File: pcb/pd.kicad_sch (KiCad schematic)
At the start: 28 parts, among them J7 Conn_01x02, U10 SGM6602-12, U11 HX4054A, U12 BQ27220, U8 TPS63051RMWR, U9 PCA9410AUKZ

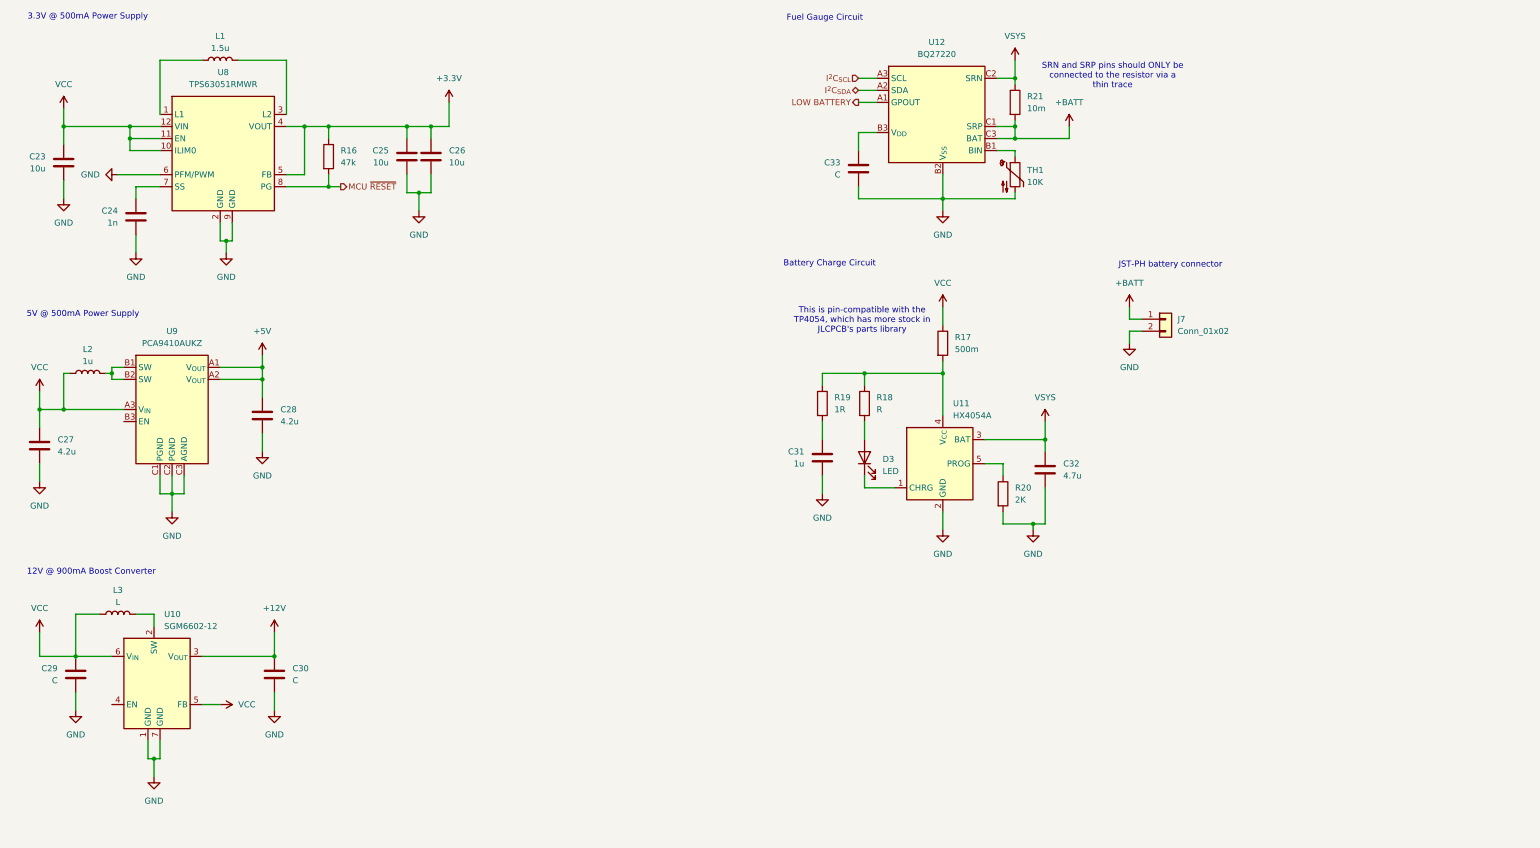
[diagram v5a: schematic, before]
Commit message: feat: revised 3.3v power rail, added power switch
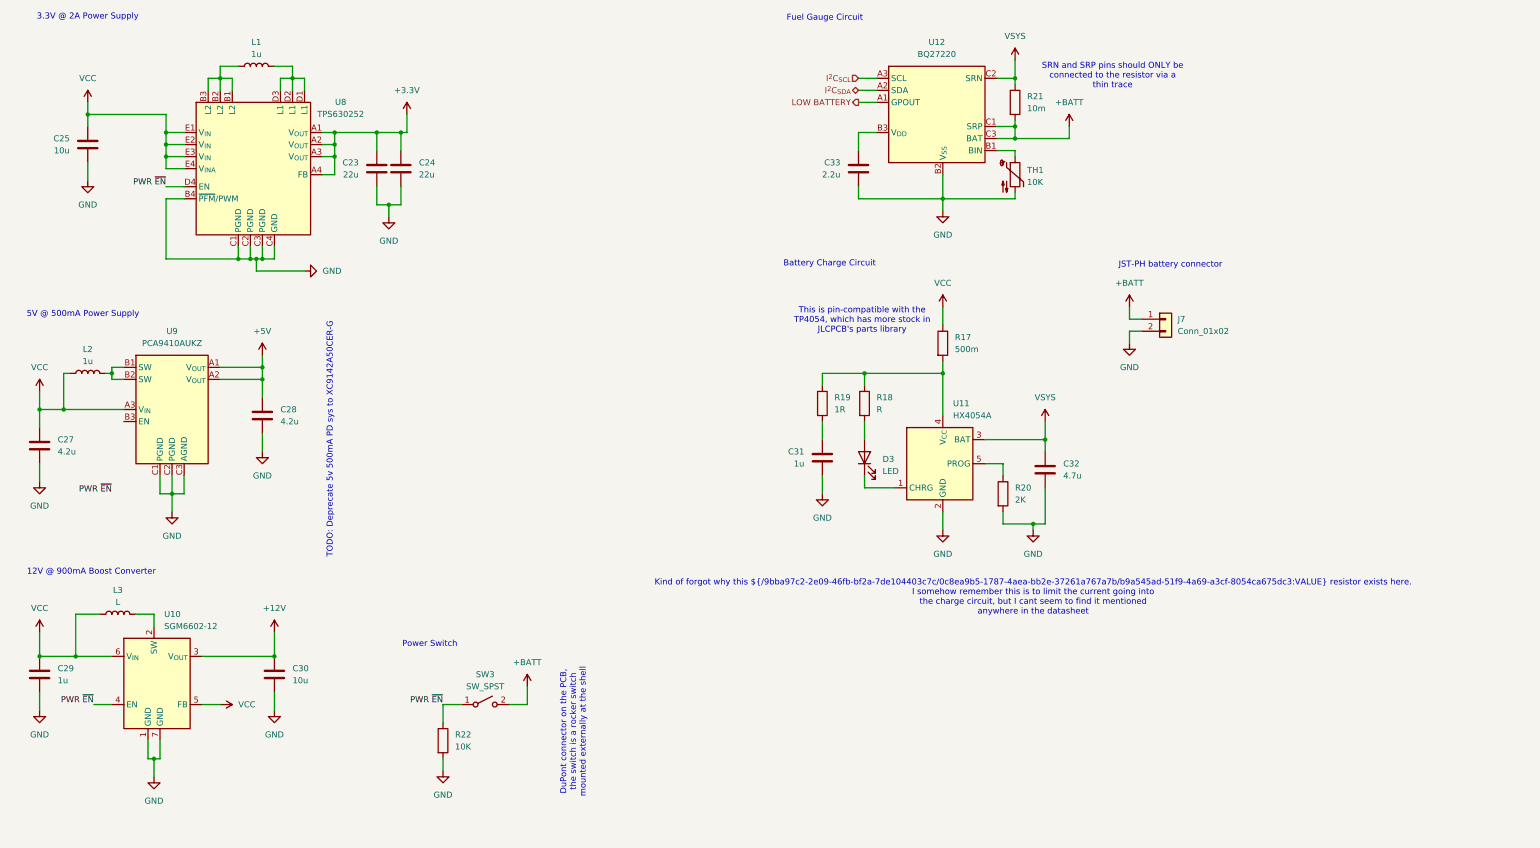
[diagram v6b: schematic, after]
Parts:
- removed C26: 10u, symbol Device:C
- removed R16: 47k, symbol Device:R
- removed U8: TPS63051RMWR, Banshee:QFN50P250X250X100-12N, symbol Banshee:TPS63051RMWR
- added R22: 10K, symbol Device:R
- added SW3: SW_SPST, Connector_PinHeader_2.54mm:PinHeader_1x02_P2.54mm_Vertical, symbol Switch:SW_SPST
- added U8: TPS630252, Banshee:YFF0020AJAF, symbol Banshee:TPS630252
- C23: value 10u -> 22u
- C24: value 1n -> 22u
- C29: value C -> 1u
- C30: value C -> 10u
- C33: value C -> 2.2u
- L1: value 1.5u -> 1u
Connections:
- net +3.3V: now also C23.1, C24.1, U8.A1 (V_{OUT}), U8.A2 (V_{OUT}), U8.A3 (V_{OUT}), U8.A4 (FB); no longer C25.1
- net +BATT: now also SW3.2 (B)
- net GND: now also R22.2, U8.B4 (~{PFM}/PWM), U8.C1 (PGND), U8.C2 (PGND), U8.C3 (PGND), U8.C4 (GND)
- net VCC: now also C25.1, U8.E1 (V_{IN}), U8.E2 (V_{IN}), U8.E3 (V_{IN}), U8.E4 (V_{INA}); no longer C23.1
- net at L1.1: now also U8.B1 (L2), U8.B2 (L2), U8.B3 (L2)
- net at L1.2: now also U8.D1 (L1), U8.D2 (L1), U8.D3 (L1)
- net PWR ~{EN}: now reaches U10.4 (EN)
- net PWR ~{EN}: now also R22.1, SW3.1 (A), U8.D4 (EN)
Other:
- note added: "3.3V @ 2A Power Supply"
- note added: "DuPont connector on the PCB, the switch is a rocker switch mounted externally at the shell"
- note added: "Kind of forgot why this ${/9bba97c2-2e09-46fb-bf2a-7de104403c7c/0c8ea9b5-1787-4aea-bb2e-37261a767a7b/b9a545ad-51f9-4a69-a3cf-8054ca675dc3:VALUE} resistor exists here. I somehow remember this is to limit the current going into the charge circuit, but I cant seem to find it mentioned anywhere in the datasheet"
- note added: "Power Switch"
- note added: "TODO: Deprecate 5v 500mA PD sys to XC9142A50CER-G"
- note removed: "3.3V @ 500mA Power Supply"
- moved on the sheet: C29

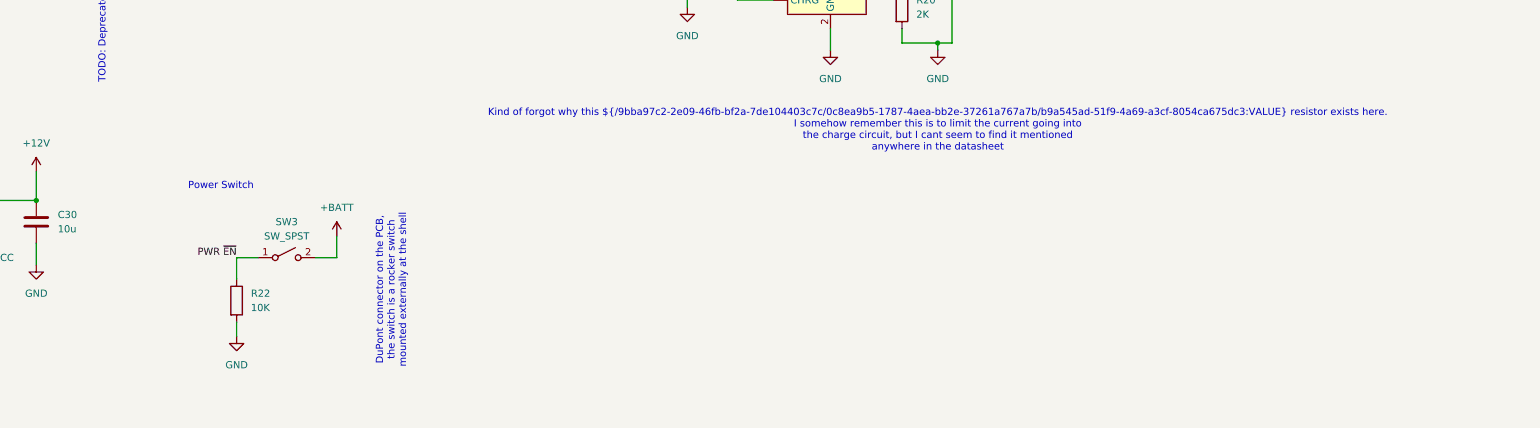
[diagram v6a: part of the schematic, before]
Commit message: feat: added documentation, updated page information
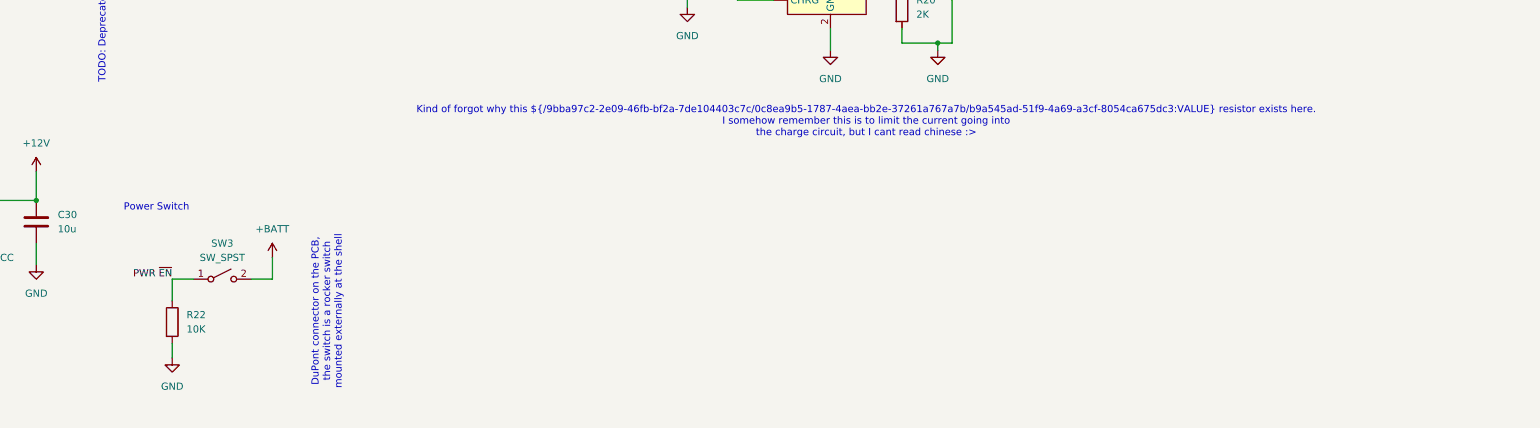
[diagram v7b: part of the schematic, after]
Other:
- note added: "Kind of forgot why this ${/9bba97c2-2e09-46fb-bf2a-7de104403c7c/0c8ea9b5-1787-4aea-bb2e-37261a767a7b/b9a545ad-51f9-4a69-a3cf-8054ca675dc3:VALUE} resistor exists here. I somehow remember this is to limit the current going into the charge circuit, but I cant read chinese :>"
- note removed: "Kind of forgot why this ${/9bba97c2-2e09-46fb-bf2a-7de104403c7c/0c8ea9b5-1787-4aea-bb2e-37261a767a7b/b9a545ad-51f9-4a69-a3cf-8054ca675dc3:VALUE} resistor exists here. I somehow remember this is to limit the current going into the charge circuit, but I cant seem to find it mentioned anywhere in the datasheet"
- moved on the sheet: R22, SW3
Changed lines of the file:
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@@
 	(text "DuPont connector on the PCB,\nthe switch is a rocker switch\nmounted externally at the shell"
 		(exclude_from_sim no)
-		(at 139.192 170.942 90)
+		(at 127.762 174.752 90)
 		(effects
 			(font
 				(size 1.27 1.27)
-				(color 0 132 0 1)
+				(color 194 0 0 1)
 			)
 		)
 	)
-	(text "Kind of forgot why this ${/9bba97c2-2e09-46fb-bf2a-7de104403c7c/0c8ea9b5-1787-4aea-bb2e-37261a767a7b/b9a545ad-51f9-4a69-a3cf-8054ca675dc3:VALUE} resistor exists here.\nI somehow remember this is to limit the current going into\nthe charge circuit, but I cant seem to find it mentioned\nanywhere in the datasheet"
+	(text "Kind of forgot why this ${/9bba97c2-2e09-46fb-bf2a-7de104403c7c/0c8ea9b5-1787-4aea-bb2e-37261a767a7b/b9a545ad-51f9-4a69-a3cf-8054ca675dc3:VALUE} resistor exists here.\nI somehow remember this is to limit the current going into\nthe charge circuit, but I cant read chinese :>"
 		(exclude_from_sim no)
-		(at 236.22 142.494 0)
+		(at 223.52 140.97 0)
 		(effects
 			(font
@@
 	(text "Power Switch"
 		(exclude_from_sim no)
-		(at 108.966 152.4 0)
+		(at 97.536 156.21 0)
 		(effects
 			(font
@@
 	(wire
 		(pts
-			(xy 129.54 165.1) (xy 125.73 165.1)
+			(xy 118.11 168.91) (xy 114.3 168.91)
 		)
 		(stroke
@@
 	(wire
 		(pts
-			(xy 111.76 176.53) (xy 111.76 179.07)
+			(xy 100.33 180.34) (xy 100.33 182.88)
 		)
 		(stroke
@@
 	(wire
 		(pts
-			(xy 111.76 165.1) (xy 111.76 168.91)
+			(xy 100.33 168.91) (xy 100.33 172.72)
 		)
 		(stroke
@@
 	(wire
 		(pts
-			(xy 129.54 161.29) (xy 129.54 165.1)
+			(xy 118.11 165.1) (xy 118.11 168.91)
 		)
 		(stroke
@@
 	(wire
 		(pts
-			(xy 115.57 165.1) (xy 111.76 165.1)
+			(xy 104.14 168.91) (xy 100.33 168.91)
 		)
 		(stroke
@@
 	)
 	(label "PWR ~{EN}"
-		(at 111.76 165.1 180)
+		(at 100.33 168.91 180)
 		(effects
 			(font
@@
 		(polyline
 			(pts
-				(xy 134.62 153.67) (xy 102.87 153.67) (xy 102.87 186.69) (xy 134.62 186.69)
+				(xy 123.19 157.48) (xy 91.44 157.48) (xy 91.44 190.5) (xy 123.19 190.5)
 			)
 			(stroke
@@
 	(symbol
 		(lib_id "Device:R")
-		(at 111.76 172.72 0)
+		(at 100.33 176.53 0)
 		(unit 1)
 		(exclude_from_sim no)
@@
 		(fields_autoplaced yes)
 		(property "Reference" "R22"
-			(at 114.3 171.4499 0)
+			(at 102.87 175.2599 0)
 			(effects
 				(font
@@
 		)
 		(property "Value" "10K"
-			(at 114.3 173.9899 0)
+			(at 102.87 177.7999 0)
 			(effects
 				(font
@@
 		)
 		(property "Footprint" ""
-			(at 109.982 172.72 90)
+			(at 98.552 176.53 90)
 			(effects
 				(font
@@
 		)
 		(property "Datasheet" "~"
-			(at 111.76 172.72 0)
+			(at 100.33 176.53 0)
 			(effects
 				(font
@@
 		)
 		(property "Description" "Resistor"
-			(at 111.76 172.72 0)
+			(at 100.33 176.53 0)
 			(effects
 				(font
@@
 	(symbol
 		(lib_id "power:GND")
-		(at 111.76 179.07 0)
+		(at 100.33 182.88 0)
 		(unit 1)
 		(exclude_from_sim no)
@@
 		(fields_autoplaced yes)
 		(property "Reference" "#PWR076"
-			(at 111.76 185.42 0)
+			(at 100.33 189.23 0)
 			(effects
 				(font
@@
 		)
 		(property "Value" "GND"
-			(at 111.76 184.15 0)
+			(at 100.33 187.96 0)
 			(effects
 				(font
@@
 		)
 		(property "Footprint" ""
-			(at 111.76 179.07 0)
+			(at 100.33 182.88 0)
 			(effects
 				(font
@@
 		)
 		(property "Datasheet" ""
-			(at 111.76 179.07 0)
+			(at 100.33 182.88 0)
 			(effects
 				(font
@@
 		)
 		(property "Description" "Power symbol creates a global label with name \"GND\" , ground"
-			(at 111.76 179.07 0)
+			(at 100.33 182.88 0)
 			(effects
 				(font
@@
 	(symbol
 		(lib_id "Switch:SW_SPST")
-		(at 120.65 165.1 0)
+		(at 109.22 168.91 0)
 		(unit 1)
 		(exclude_from_sim no)
@@
 		(fields_autoplaced yes)
 		(property "Reference" "SW3"
-			(at 120.65 158.75 0)
+			(at 109.22 162.56 0)
 			(effects
 				(font
@@
 		)
 		(property "Value" "SW_SPST"
-			(at 120.65 161.29 0)
+			(at 109.22 165.1 0)
 			(effects
 				(font
@@
 		)
 		(property "Footprint" "Connector_PinHeader_2.54mm:PinHeader_1x02_P2.54mm_Vertical"
-			(at 120.65 165.1 0)
+			(at 109.22 168.91 0)
 			(effects
 				(font
@@
 		)
 		(property "Datasheet" "~"
-			(at 120.65 165.1 0)
+			(at 109.22 168.91 0)
 			(effects
 				(font
@@
 		)
 		(property "Description" "Single Pole Single Throw (SPST) switch"
-			(at 120.65 165.1 0)
+			(at 109.22 168.91 0)
 			(effects
 				(font
@@
 	(symbol
 		(lib_id "power:+BATT")
-		(at 129.54 161.29 0)
+		(at 118.11 165.1 0)
 		(unit 1)
 		(exclude_from_sim no)
@@
 		(fields_autoplaced yes)
 		(property "Reference" "#PWR073"
-			(at 129.54 165.1 0)
+			(at 118.11 168.91 0)
 			(effects
 				(font
@@
 		)
 		(property "Value" "+BATT"
-			(at 129.54 156.21 0)
+			(at 118.11 160.02 0)
 			(effects
 				(font
@@
 		)
 		(property "Footprint" ""
-			(at 129.54 161.29 0)
+			(at 118.11 165.1 0)
 			(effects
 				(font
@@
 		)
 		(property "Datasheet" ""
-			(at 129.54 161.29 0)
+			(at 118.11 165.1 0)
 			(effects
 				(font
@@
 		)
 		(property "Description" "Power symbol creates a global label with name \"+BATT\""
-			(at 129.54 161.29 0)
+			(at 118.11 165.1 0)
 			(effects
 				(font

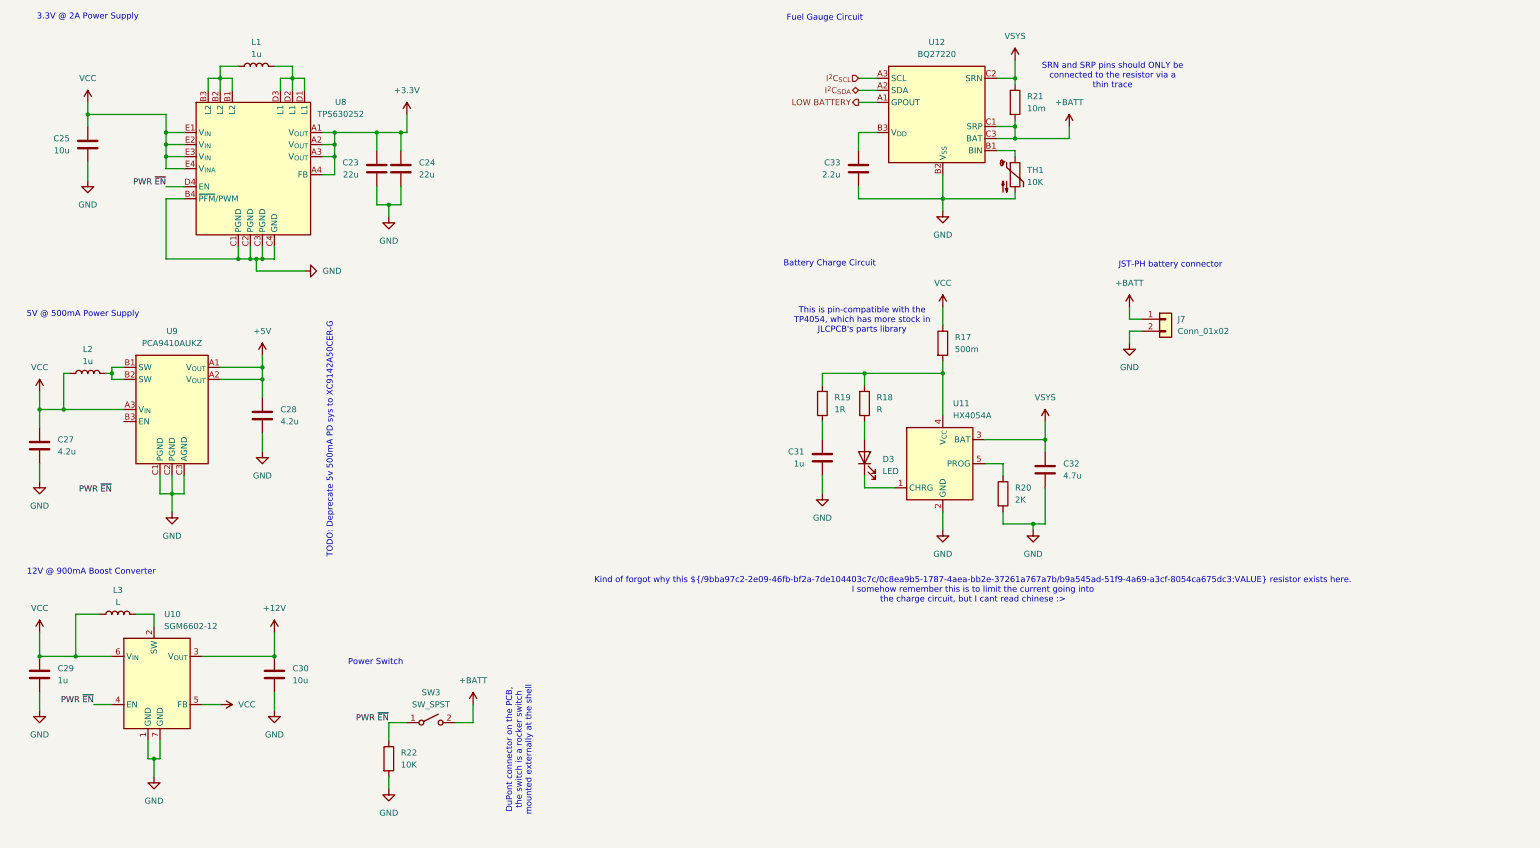
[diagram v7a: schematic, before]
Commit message: chore: re-annotated schematic symbols
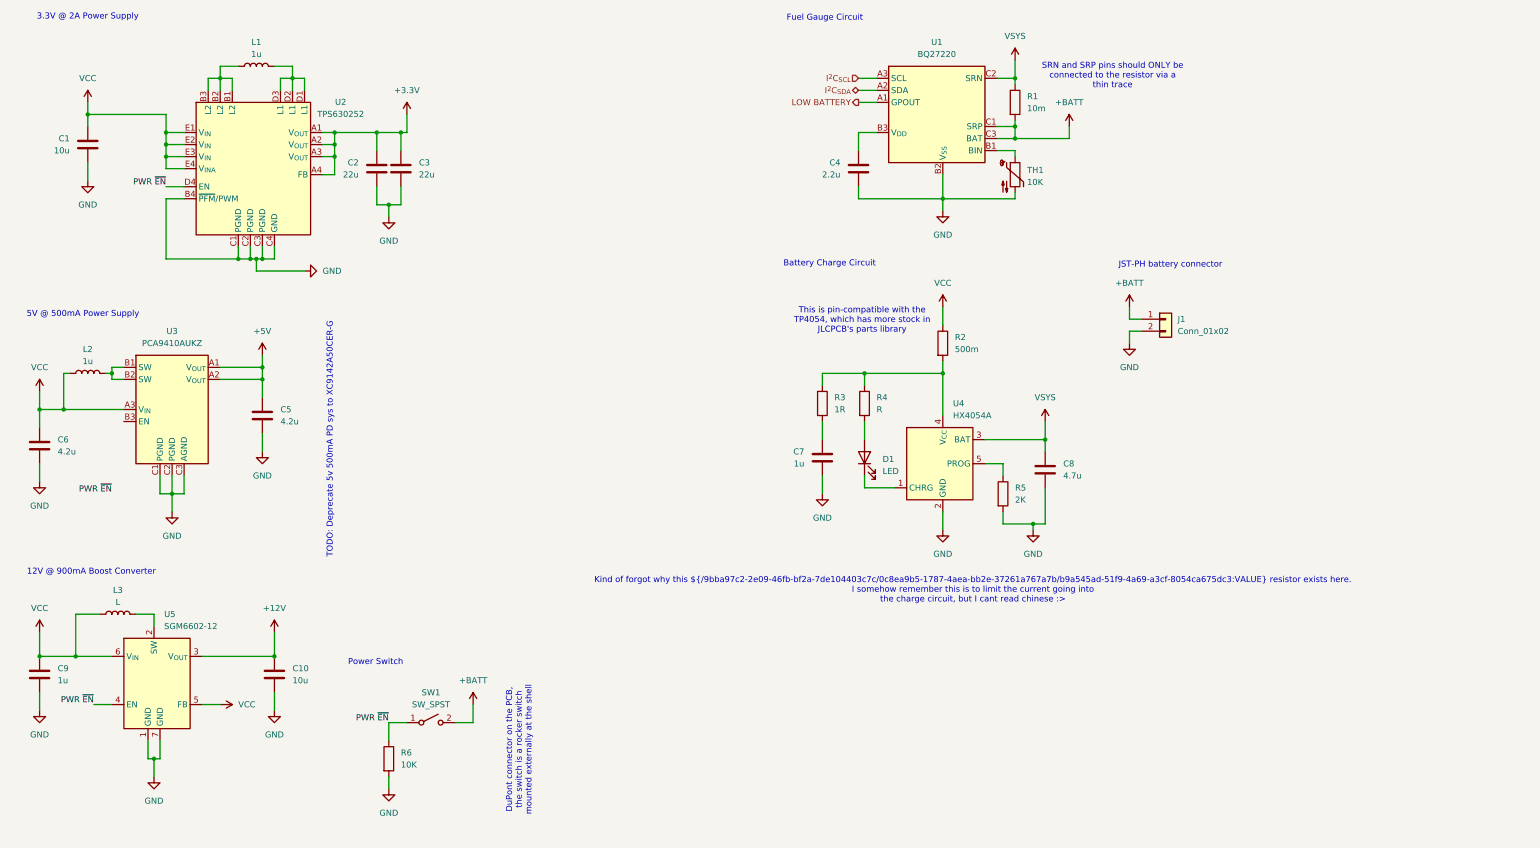
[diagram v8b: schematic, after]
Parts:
- renumbered C25 to C1, C30 to C10, C23 to C2, C24 to C3, C33 to C4, C28 to C5, C27 to C6, C31 to C7, C32 to C8, C29 to C9, D3 to D1, J7 to J1, R21 to R1, R17 to R2, R19 to R3, R18 to R4, R20 to R5, R22 to R6, SW3 to SW1, U12 to U1, U8 to U2, U9 to U3, U11 to U4, U10 to U5
